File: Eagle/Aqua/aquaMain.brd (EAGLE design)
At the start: 100 x 80 mm, 41 parts, among them IC1 ATMEGA168-20P, IC2 DS1307, IC3 74HC125N, IC4 L7805CV, IC5 LF33CV, IC6 PCF8574P, IC7 24LC256P, IC8 40106N, J1 POWER_JACKSLT, T1 BC337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

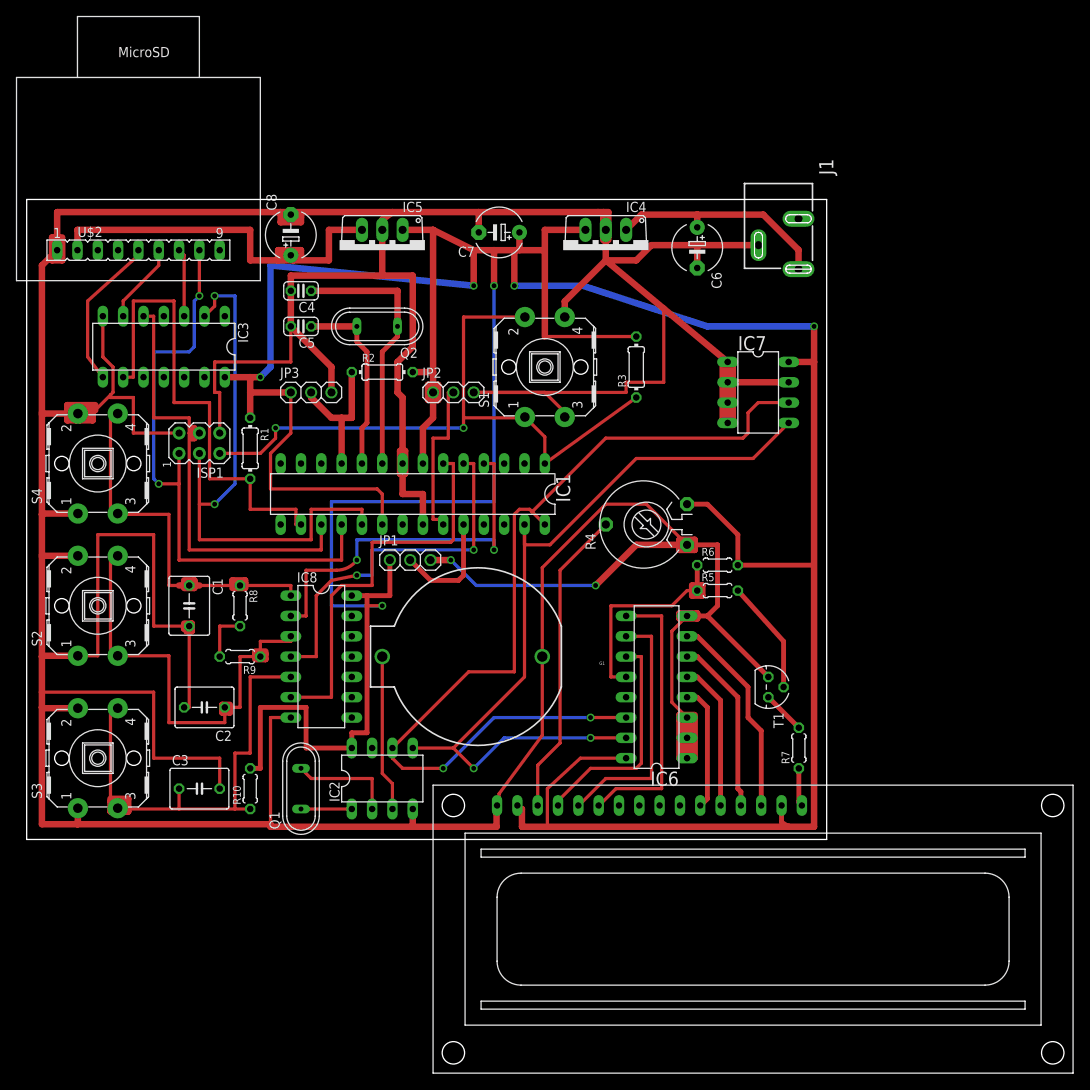
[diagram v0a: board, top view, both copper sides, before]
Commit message: Filled empty spaces with copper (faster eatching) Redone ArduinoNANO to DIP28 PCB to a single-side version Added V1 printout image
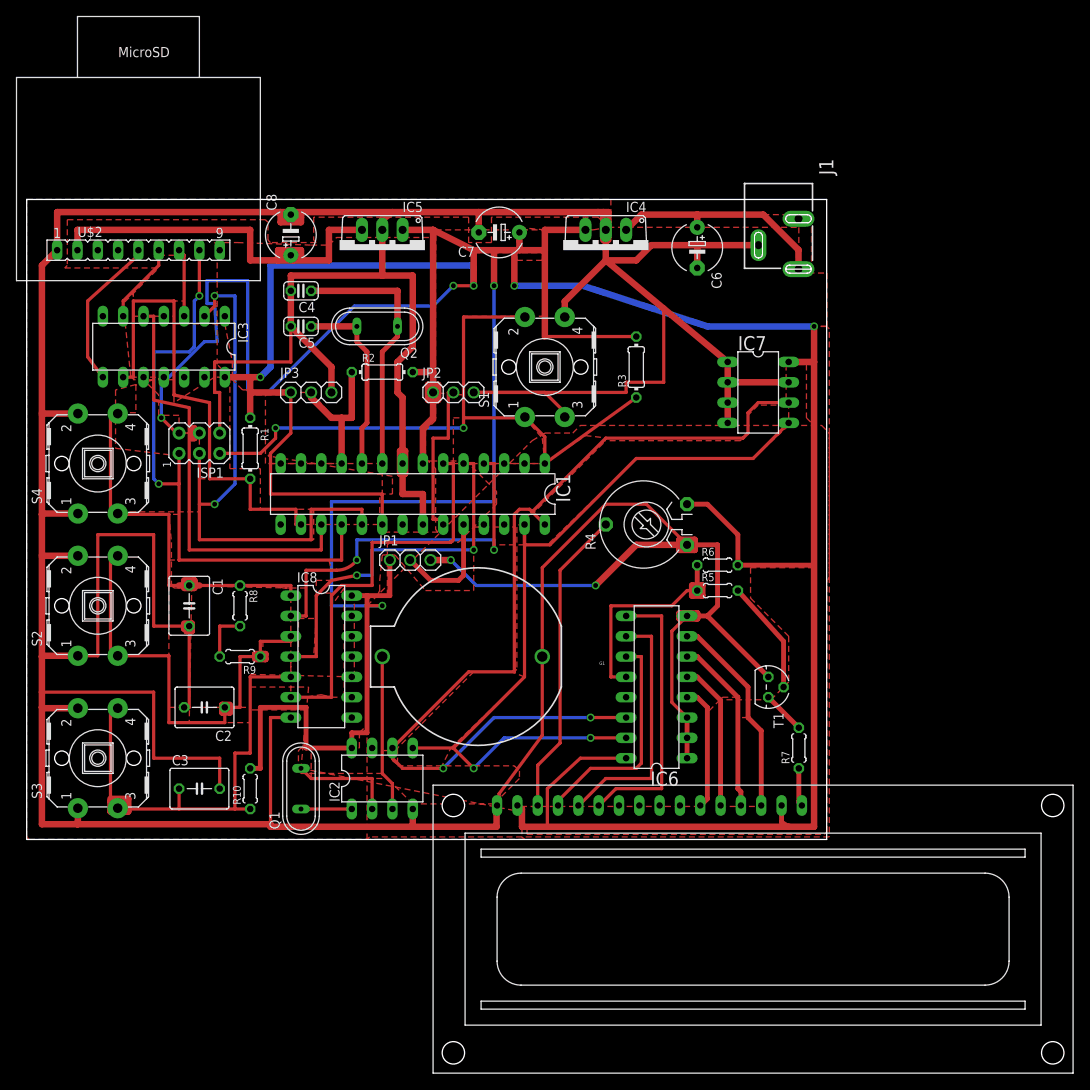
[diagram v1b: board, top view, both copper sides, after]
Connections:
- net N$25: now also ISP1.2
- net VSS: no longer ISP1.2
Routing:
- net N$25: track 522.9 -> 603.1 mm, vias 6 -> 8
- net VSS: track 765.4 -> 718.7 mm
- net N$30: track 27.3 -> 0.00 mm
- net N$26: track 16.5 -> 1.27 mm
- net N$31: track 7.94 -> 0.00 mm
- net N$46: track 6.03 -> 0.00 mm
- net N$47: track 1.27 -> 0.00 mm
- net N$18: track 59.7 -> 58.8 mm
- net N$14: track 59.7 -> 58.8 mm
- added copper zone on layer 1, net N$1
- added copper zone on layer 1, net N$10
- added copper zone on layer 1, net N$14
- added copper zone on layer 1, net N$18
- added copper zone on layer 1, net N$20
- added copper zone on layer 1, net N$21
- added copper zone on layer 1, net N$25
- added copper zone on layer 1, net N$3
- added copper zone on layer 1, net N$34
- added copper zone on layer 1, net N$43
- added copper zone on layer 1, net N$44
- added copper zone on layer 1, net N$8
- added copper zone on layer 1, net N@16
- added copper zone on layer 1, net VSS

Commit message: Big update Many important fixes dictated by 1st prototype
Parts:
- added JP4: (no value), pinhead:1X02
- added LED1, LED2, LED3: (no value), SparkFun-LED:LED3MM
- added S5: (no value), SparkFun-Electromechanical:TACTILE-PTH
- moved C6 5.72 mm to (78.1, 74.3)
- moved T1 5.40 mm to (95.2, 23.8), turned to 180 degrees
- moved C8 4.32 mm to (37.1, 74.3)
- moved IC4 3.81 mm to (68.6, 76.2)
- moved IC5 1.59 mm to (46.0, 76.2)
- moved C7 1.31 mm to (57.8, 76.2)
- moved J1 1.14 mm to (100.0, 85.7)
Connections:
- removed net +5V: R8.2, R9.2
- removed net N$1: C6.+, IC4.VIN, J1.PWR
- new net N$31: J1.PWR, LED3.A, S5.1, S5.2
- new net N$46: C6.+, IC4.VIN, S5.3, S5.4
- new net N$56: IC1.2, JP4.1
- new net N$57: IC1.3, JP4.2
- net N$22: now also LED2.A
- net N$25: now also LED1.A, R8.2, R9.2
- net N$42: now also T1.3; no longer T1.1
- net VSS: now also LED1.K, LED2.K, LED3.K, T1.1; no longer T1.3
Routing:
- net N$25: track 603.1 -> 638.0 mm, vias 8 -> 16
- net N$1: track 28.2 -> 0.00 mm
- net N$31: track 0.00 -> 25.5 mm
- net N$46: track 0.00 -> 19.7 mm
- net N$43: track 51.9 -> 39.0 mm
- net N$22: track 54.0 -> 42.9 mm
- net N$45: track 66.3 -> 56.1 mm
- net N$48: track 7.94 -> 0.00 mm
- net N$44: track 61.9 -> 54.7 mm
- net N$27: track 6.98 -> 0.00 mm
- net +5V: track 6.35 -> 0.00 mm
- net N$28: track 5.08 -> 0.00 mm
- net N$42: track 5.39 -> 9.84 mm
- net N$57: track 0.00 -> 4.41 mm
- net N$56: track 0.00 -> 4.41 mm
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
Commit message: - important fix to SD wiring (not implemented in PCB yet) - SD logging function in arduino project
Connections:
- net VSS: now also IC3.1, IC3.10, IC3.4
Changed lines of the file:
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@@
 <via x="52.705" y="34.925" extent="1-16" drill="0.6" diameter="1.778" shape="square"/>
 <contactref element="T1" pad="1"/>
+<contactref element="IC3" pad="1"/>
+<contactref element="IC3" pad="4"/>
+<contactref element="IC3" pad="10"/>
+<wire x1="86.36" y1="29.21" x2="93.98" y2="23.8125" width="0" layer="19" extent="1-1"/>
+<wire x1="14.605" y1="57.785" x2="10.795" y2="60.0075" width="0" layer="19" extent="1-1"/>
+<wire x1="24.765" y1="65.405" x2="23.495" y2="59.69" width="0" layer="19" extent="1-1"/>
+<wire x1="17.145" y1="65.405" x2="9.525" y2="65.405" width="0" layer="19" extent="1-1"/>
 </signal>
 <signal name="N$6">

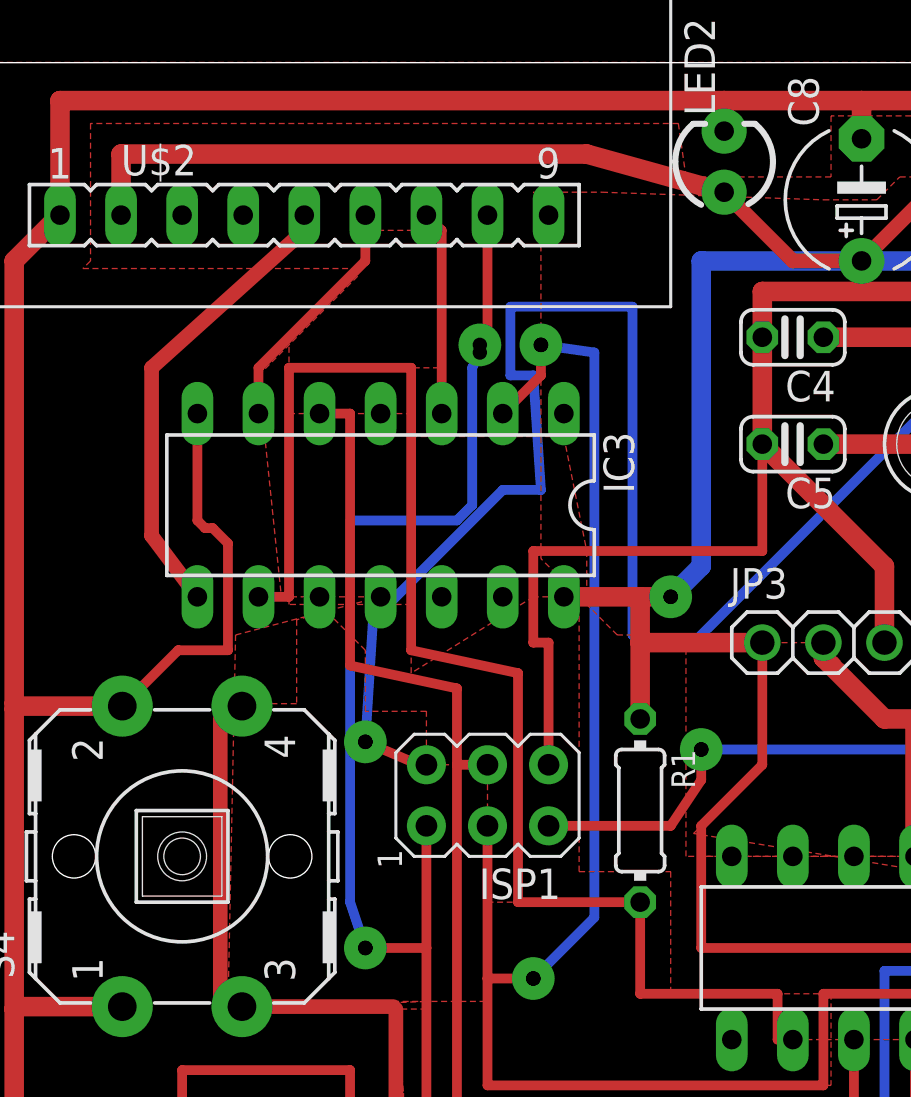
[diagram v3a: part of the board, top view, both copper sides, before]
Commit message: Final project commit: - prototype proven to working continously for 4 months as of 1/8/15 - added pictures - [1/5/15] improvement - decrease R2 to 2.2kOhm, improved SNR from DS18B20 - project finished
Achieved:
- LCD display over i2c interface
- Functional 3-button menu English and Polish
- Ph probe reading with calibration code
- EEPROM save of Ph calibration
- Temperature reading [DS18B20]
- Data and clock [DS1307]
- SD card logging

Signed-off-by: pradyjowski <patryk.radyjowski@gmail.com>
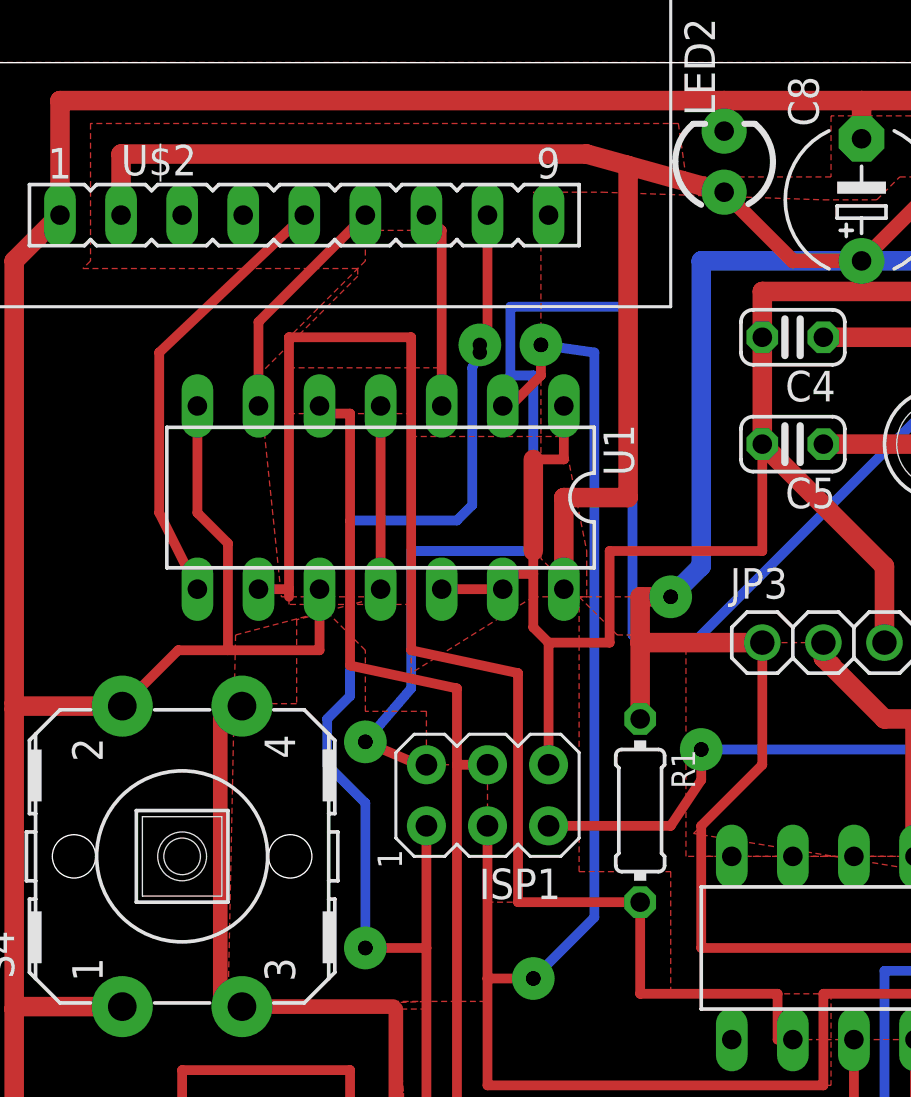
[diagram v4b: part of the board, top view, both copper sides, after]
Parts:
- removed IC3: 74HC125N, 74xx-eu:DIL14
- added U1: 74AHC125, dedicatedLib:DIP14
- R2: value 4.7k -> 2.2k
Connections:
- new net N$58: U1.11, U1.4
- net N$14: now also U1.5; no longer IC3.5
- net N$15: now also IC1.16, R1.2, U1.9; no longer IC3.6, U$2.6
- net N$16: now also U1.2; no longer IC3.2
- net N$17: now also U1.3; no longer IC3.3
- net N$18: now also U$2.5, U1.8; no longer IC1.16, IC3.9, R1.2
- net N$19: now also U$2.6, U1.6; no longer IC3.8, U$2.5
- net N$22: now also U1.14
- net N$25: no longer IC3.14
- net VSS: now also U1.1, U1.10, U1.12, U1.13, U1.7; no longer IC3.1, IC3.10, IC3.4, IC3.7
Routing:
- net N$15: track 10.7 -> 61.4 mm
- net N$18: track 58.8 -> 18.5 mm
- net VSS: track 716.3 -> 737.4 mm
- net N$22: track 42.9 -> 63.2 mm
- net N$19: track 19.3 -> 9.78 mm
- net N$58: track 0.00 -> 7.62 mm
- net N$25: track 638.0 -> 636.8 mm
- net N$13: track 76.3 -> 77.3 mm
